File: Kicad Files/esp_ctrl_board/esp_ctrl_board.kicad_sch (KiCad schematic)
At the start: 10 parts, among them U1 ESP32-WROOM-32

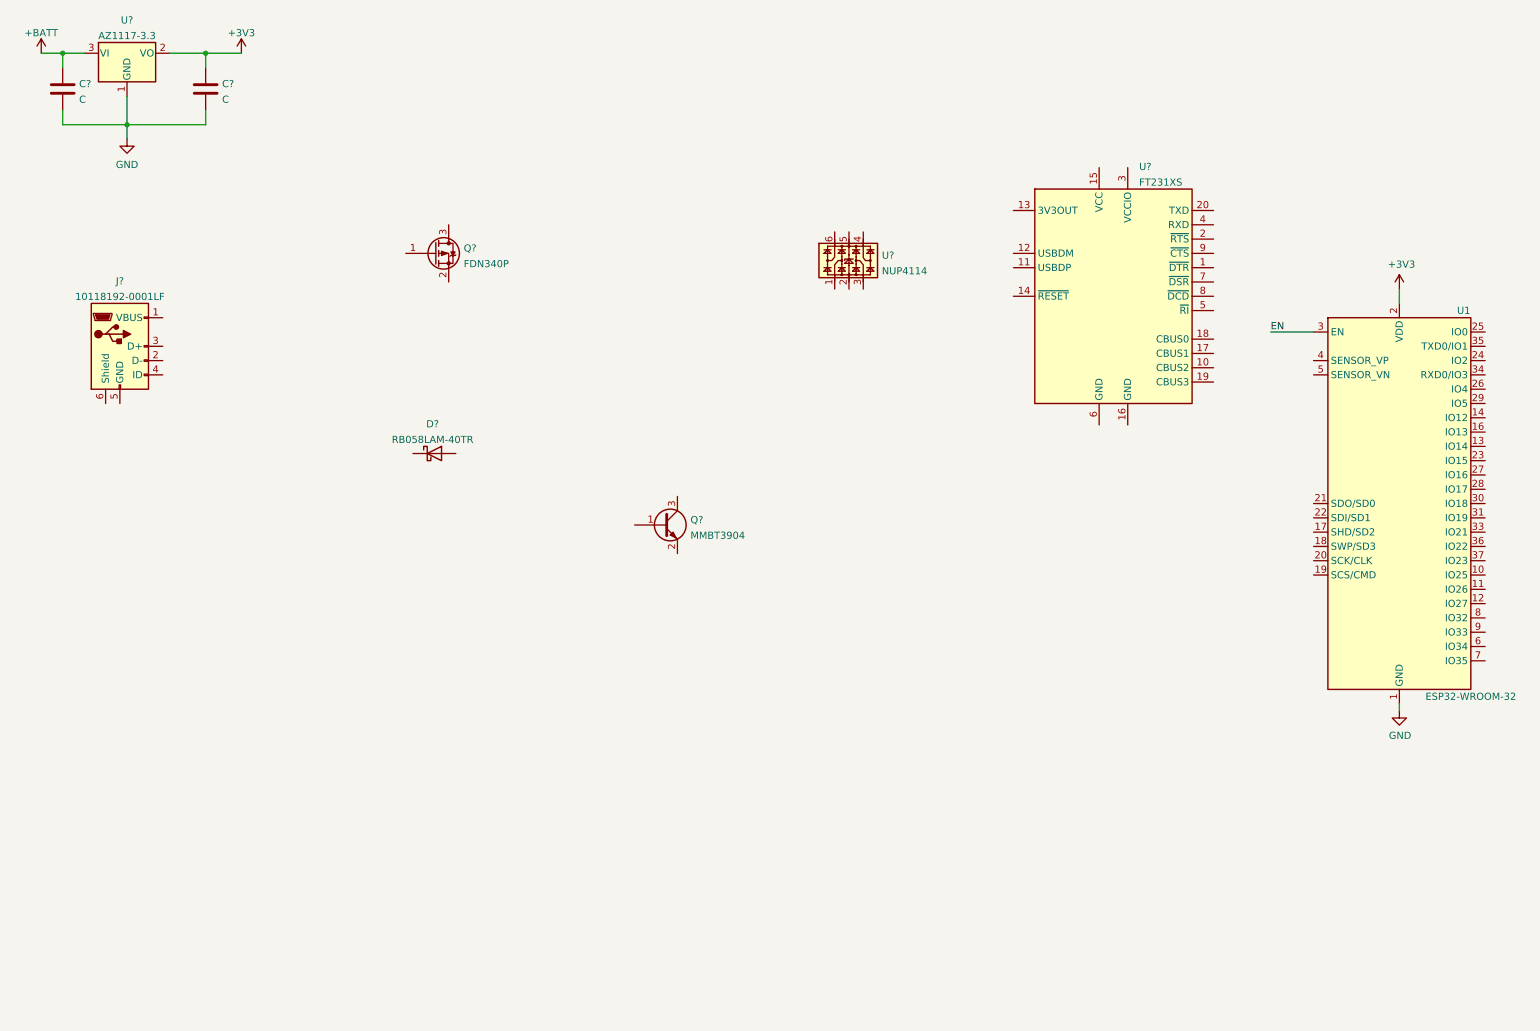
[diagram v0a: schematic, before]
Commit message: Completed USB-UART circuit design, starting on power distribution
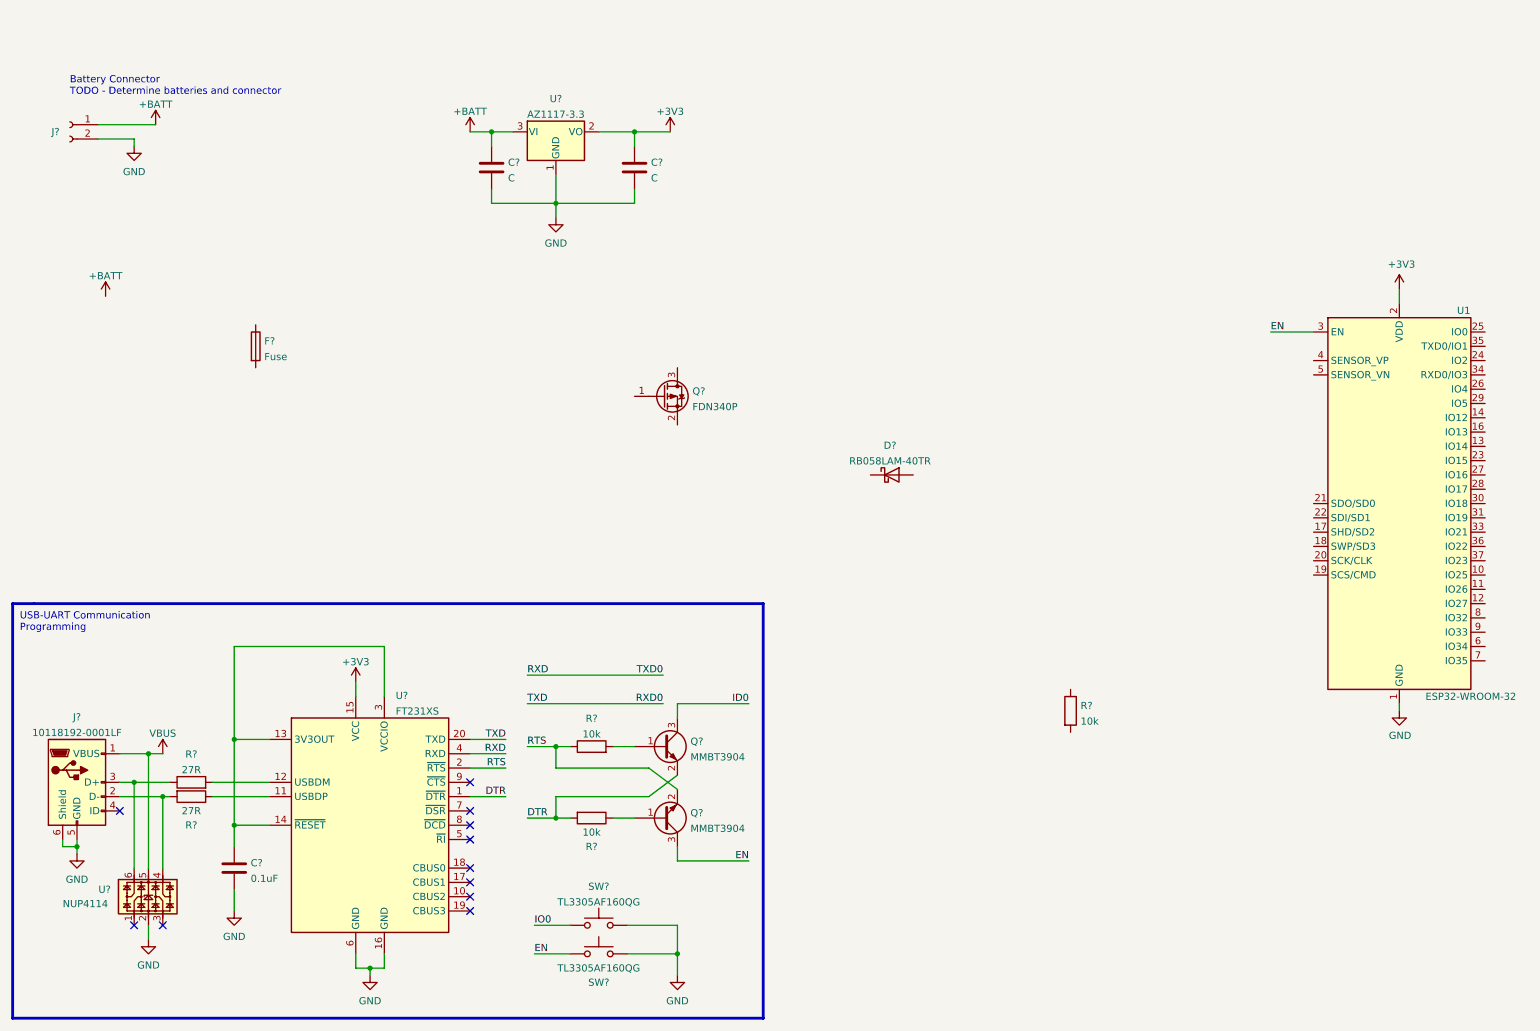
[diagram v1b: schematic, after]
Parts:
- added C?: 0.1uF, Capacitor_SMD:C_0603_1608Metric_Pad1.08x0.95mm_HandSolder, symbol Device:C
- added F?: Fuse, Fuse:Fuseholder_Blade_Mini_Keystone_3568, symbol Device:Fuse
- added J?: Conn_01x02_Female, symbol Connector:Conn_01x02_Female
- added Q?: MMBT3904, Package_TO_SOT_SMD:SOT-23, symbol Transistor_BJT:MMBT3904
- added R? (x2): 27R, Resistor_SMD:R_0603_1608Metric_Pad0.98x0.95mm_HandSolder, symbol Device:R
- added R? (x3): 10k, Resistor_SMD:R_0603_1608Metric_Pad0.98x0.95mm_HandSolder, symbol Device:R
- added SW? (x2): TL3305AF160QG, Button_Switch_SMD:SW_SPST_B3SL-1002P, symbol Switch:SW_MEC_5G
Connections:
- net +3V3: now also U?.15 (VCC)
- net +BATT: now also J?.1 (Pin_1)
- net EN: now also Q?.3 (C), SW?.1 (A), SW?.2 (A)
- net GND: now also J?.5 (GND), J?.6 (Shield), U?.16 (GND), U?.2, U?.6 (GND), C?.2, J?.2 (Pin_2), SW?.3 (B), SW?.3 (B), SW?.4 (B), SW?.4 (B)
- net at U?.4: now also J?.2 (D-), R?.2
- net VBUS: now reaches U?.5
- net VBUS: now also J?.1 (VBUS)
- net at U?.6: now also J?.3 (D+), R?.1
- net at Q?.1 (B): now also R?.2
- net DTR: now reaches Q?.2 (E)
- net DTR: now also U?.1 (~{DTR}), R?.2
- net ID0: now reaches Q?.3 (C)
- net at U?.11 (USBDP): now also R?.1
- net at U?.12 (USBDM): now also R?.2
- net at U?.13 (3V3OUT): now also U?.14 (~{RESET}), U?.3 (VCCIO), C?.1
- net RTS: now reaches U?.2 (~{RTS})
- net RTS: now also Q?.2 (E), R?.1
- net RXD0: now reaches U?.20 (TXD)
- net RXD: now reaches U?.4 (RXD)
- new net: Q?.1 (B), R?.1
- new net IO0: SW?.1 (A), SW?.2 (A)
- no-connect marks 0 -> 11
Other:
- note added: "Battery Connector TODO - Determine batteries and connector"
- note added: "USB-UART Communication Programming"
- moved on the sheet: C?, D?, J?, Q?, U?

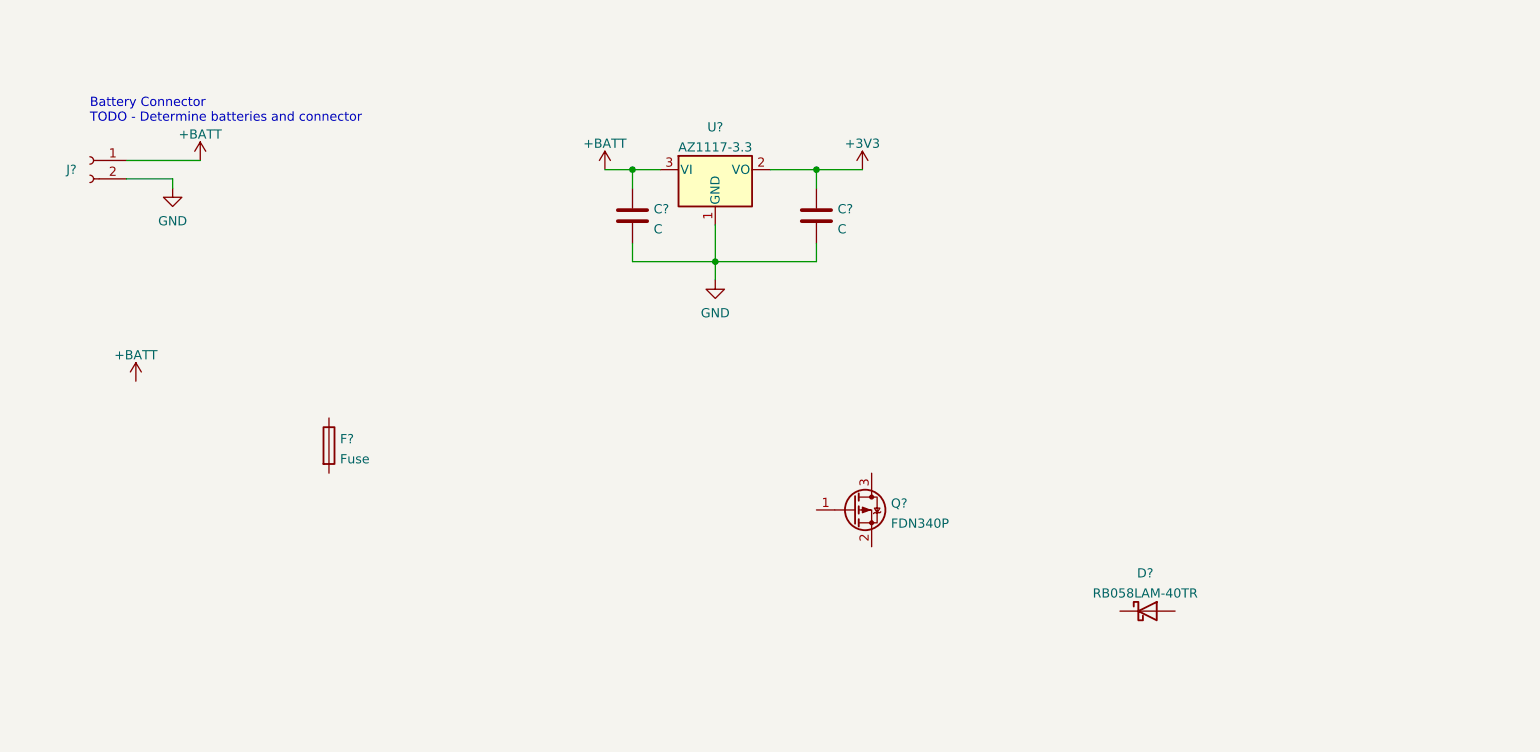
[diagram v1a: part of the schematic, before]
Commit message: Exploring new design for power
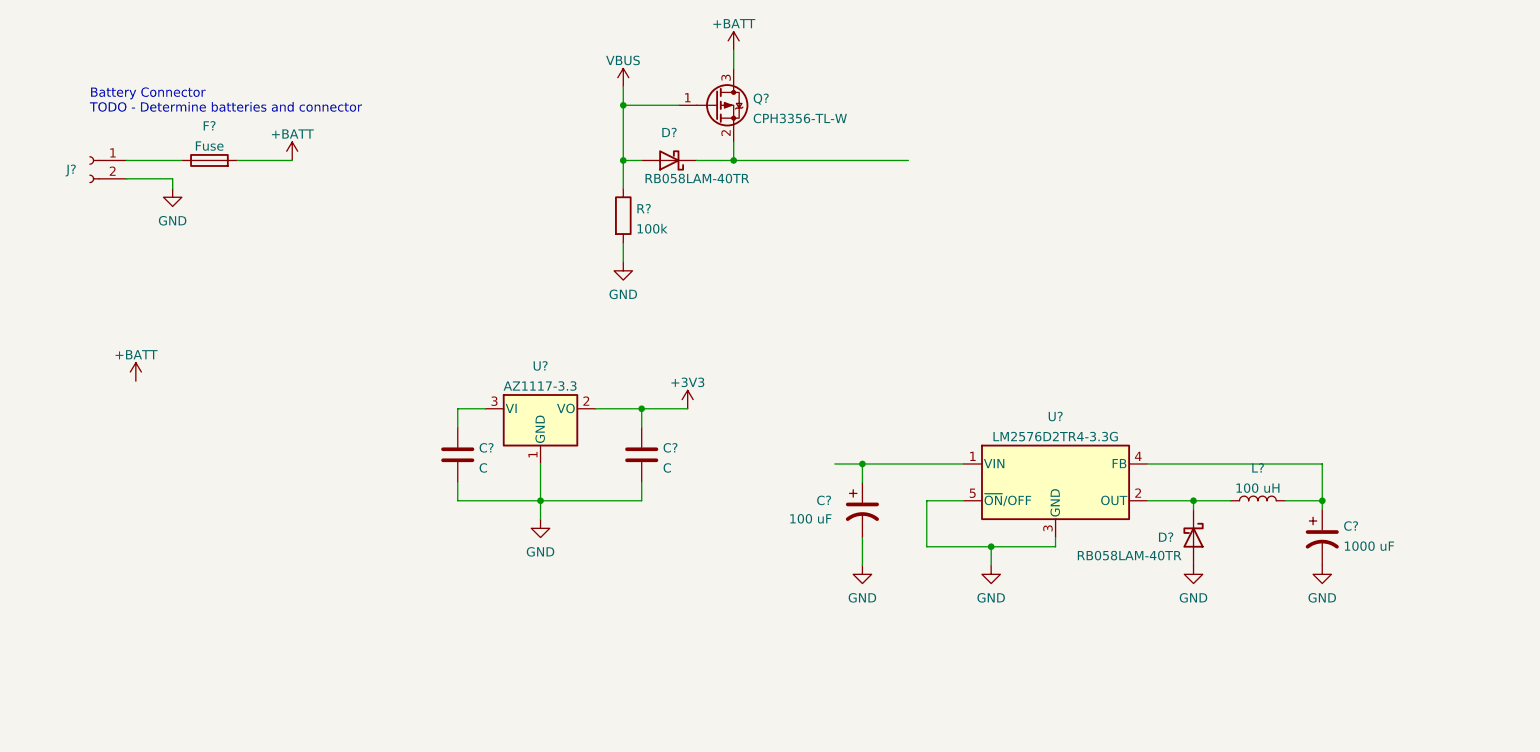
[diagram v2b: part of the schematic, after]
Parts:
- added C?: 100 uF, symbol Device:C_Polarized_US
- added C?: 1000 uF, symbol Device:C_Polarized_US
- added D?: RB058LAM-40TR, Diode_SMD:D_SOD-128, symbol Device:D_Schottky
- added L?: 100 uH, symbol Device:L
- added R?: 100k, Resistor_SMD:R_0603_1608Metric_Pad0.98x0.95mm_HandSolder, symbol Device:R
- added U?: LM2576D2TR4-3.3G, Package_TO_SOT_SMD:TO-263-5_TabPin3, symbol Regulator_Switching:LM2576HVS-3.3
- Q?: value FDN340P -> CPH3356-TL-W; footprint Package_TO_SOT_SMD:SOT-23 -> Package_TO_SOT_SMD:SC-59_Handsoldering; Purchase Link https://www.digikey.com/en/products/detail/on-semiconductor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 -> https://www.digikey.com/en/products/detail/onsemi/CPH3356-T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
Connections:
- net +BATT: now also F?.2, Q?.3 (D); no longer C?.1, J?.1 (Pin_1), U?.3 (VI)
- net GND: now also C?.2, C?.2, D?.2 (A), R?.2, U?.3 (GND), U?.5 (~{ON}/OFF)
- net VBUS: now also D?.2 (A), Q?.1 (G), R?.1
- net at F?.1: now also J?.1 (Pin_1)
- net at D?.1 (K): now also Q?.2 (S)
- new net: C?.1, U?.1 (VIN)
- new net: D?.1 (K), L?.1, U?.2 (OUT)
- new net: C?.1, L?.2, U?.4 (FB)
- new net: C?.1, U?.3 (VI)
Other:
- moved on the sheet: C?, D?, F?, Q?, U?

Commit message: More power design configurations
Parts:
- added U?: ADP2303ARDZ-3.3, Package_SO:SOIC-8-1EP_3.9x4.9mm_P1.27mm_EP2.29x3mm, symbol Regulator_Switching:ADP2303ARDZ-3.3
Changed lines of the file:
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@@
     (pin "3")
+  )
+  (symbol (lib_id "Regulator_Switching:ADP2303ARDZ-3.3") (at 172.72 50.8 0) (unit 1)
+    (in_bom yes) (on_board yes) (fields_autoplaced)
+    (property "Reference" "U?" (id 0) (at 172.72 39.2135 0))
+    (property "Value" "ADP2303ARDZ-3.3" (id 1) (at 172.72 41.9886 0))
+    (property "Footprint" "Package_SO:SOIC-8-1EP_3.9x4.9mm_P1.27mm_EP2.29x3mm" (id 2) (at 176.53 59.69 0)
+      (effects (font (size 1.27 1.27)) (justify left) hide)
+    )
+    (property "Datasheet" "https://www.analog.com/media/en/technical-documentation/data-sheets/ADP2302_2303.pdf" (id 3) (at 167.64 35.56 0)
+      (effects (font (size 1.27 1.27)) hide)
+    )
+    (pin "1")
+    (pin "2")
+    (pin "3")
+    (pin "4")
+    (pin "5")
+    (pin "6")
+    (pin "7")
+    (pin "8")
+    (pin "9")
   )
   (symbol (lib_id "Device:R") (at 116.84 147.32 90) (unit 1)
@@
       (reference "U?") (unit 1) (value "FT231XS") (footprint "Package_SO:SSOP-20_3.9x8.7mm_P0.635mm")
     )
-  )
+    (path "/e683c66c-27ed-4f39-8b08-e2022568a643"
+      (reference "U?") (unit 1) (value "ADP2303ARDZ-3.3") (footprint "Package_SO:SOIC-8-1EP_3.9x4.9mm_P1.27mm_EP2.29x3mm")
+    )
+  )
